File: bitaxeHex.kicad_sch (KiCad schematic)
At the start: 8 parts, among them J1 Conn_01x01, J2 Conn_01x01

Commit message: hex initial import
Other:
- sheet BM1397 renamed BM1397-1
- added sheet BM1397-3 (bm1397-3.kicad_sch)
- added sheet BM1398-2 (bm1397-2.kicad_sch)
- sheet BM1397-1: file bm1397.kicad_sch -> bm1397-1.kicad_sch
- sheet Fan ports: added TEMP1_N, TEMP1_P, TEMP2_N, TEMP2_P; removed TEMP_N, TEMP_P
- title: le bitaxeMax -> bitaxeHex
- moved on the sheet: H1, H2, H3, H4, H5, H6

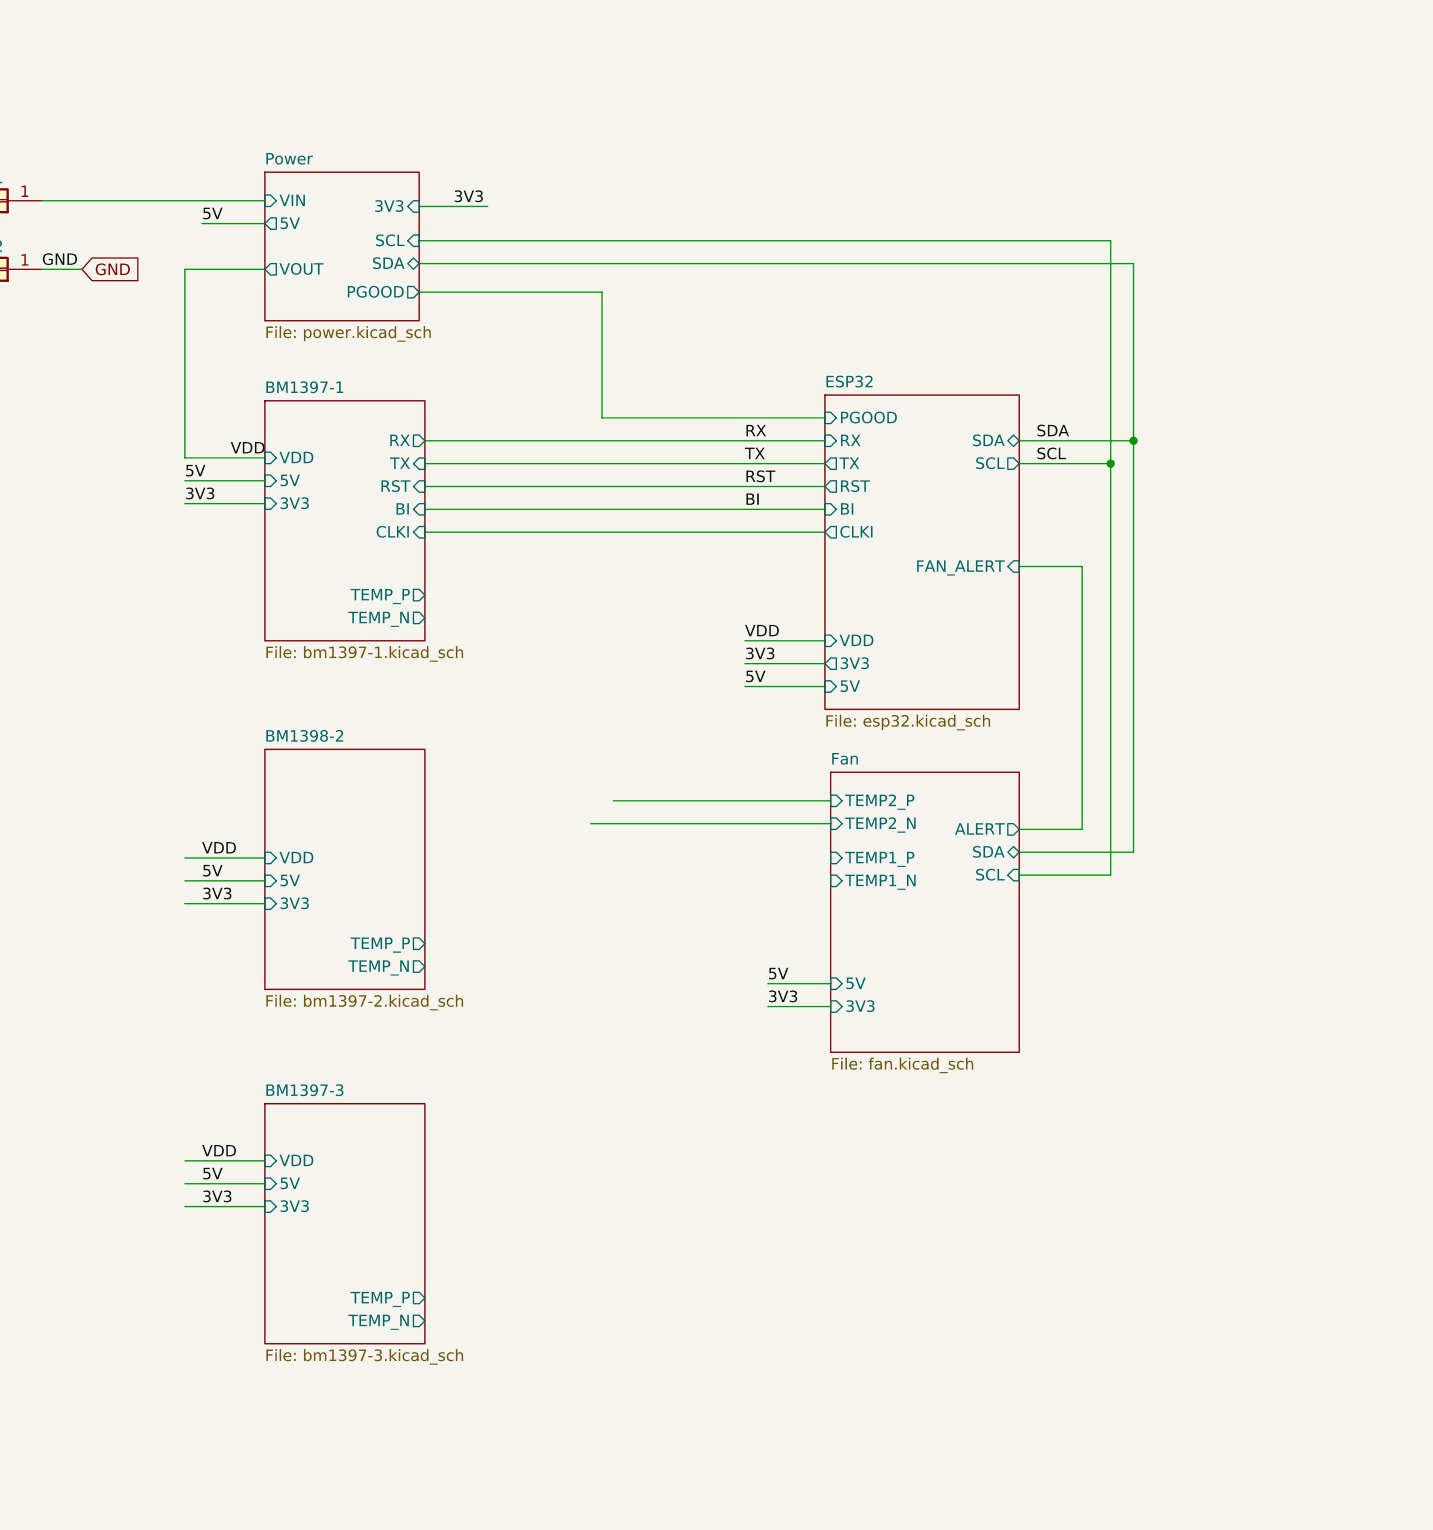
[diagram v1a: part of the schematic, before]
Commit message: connected up power and data to ASICs in schematic
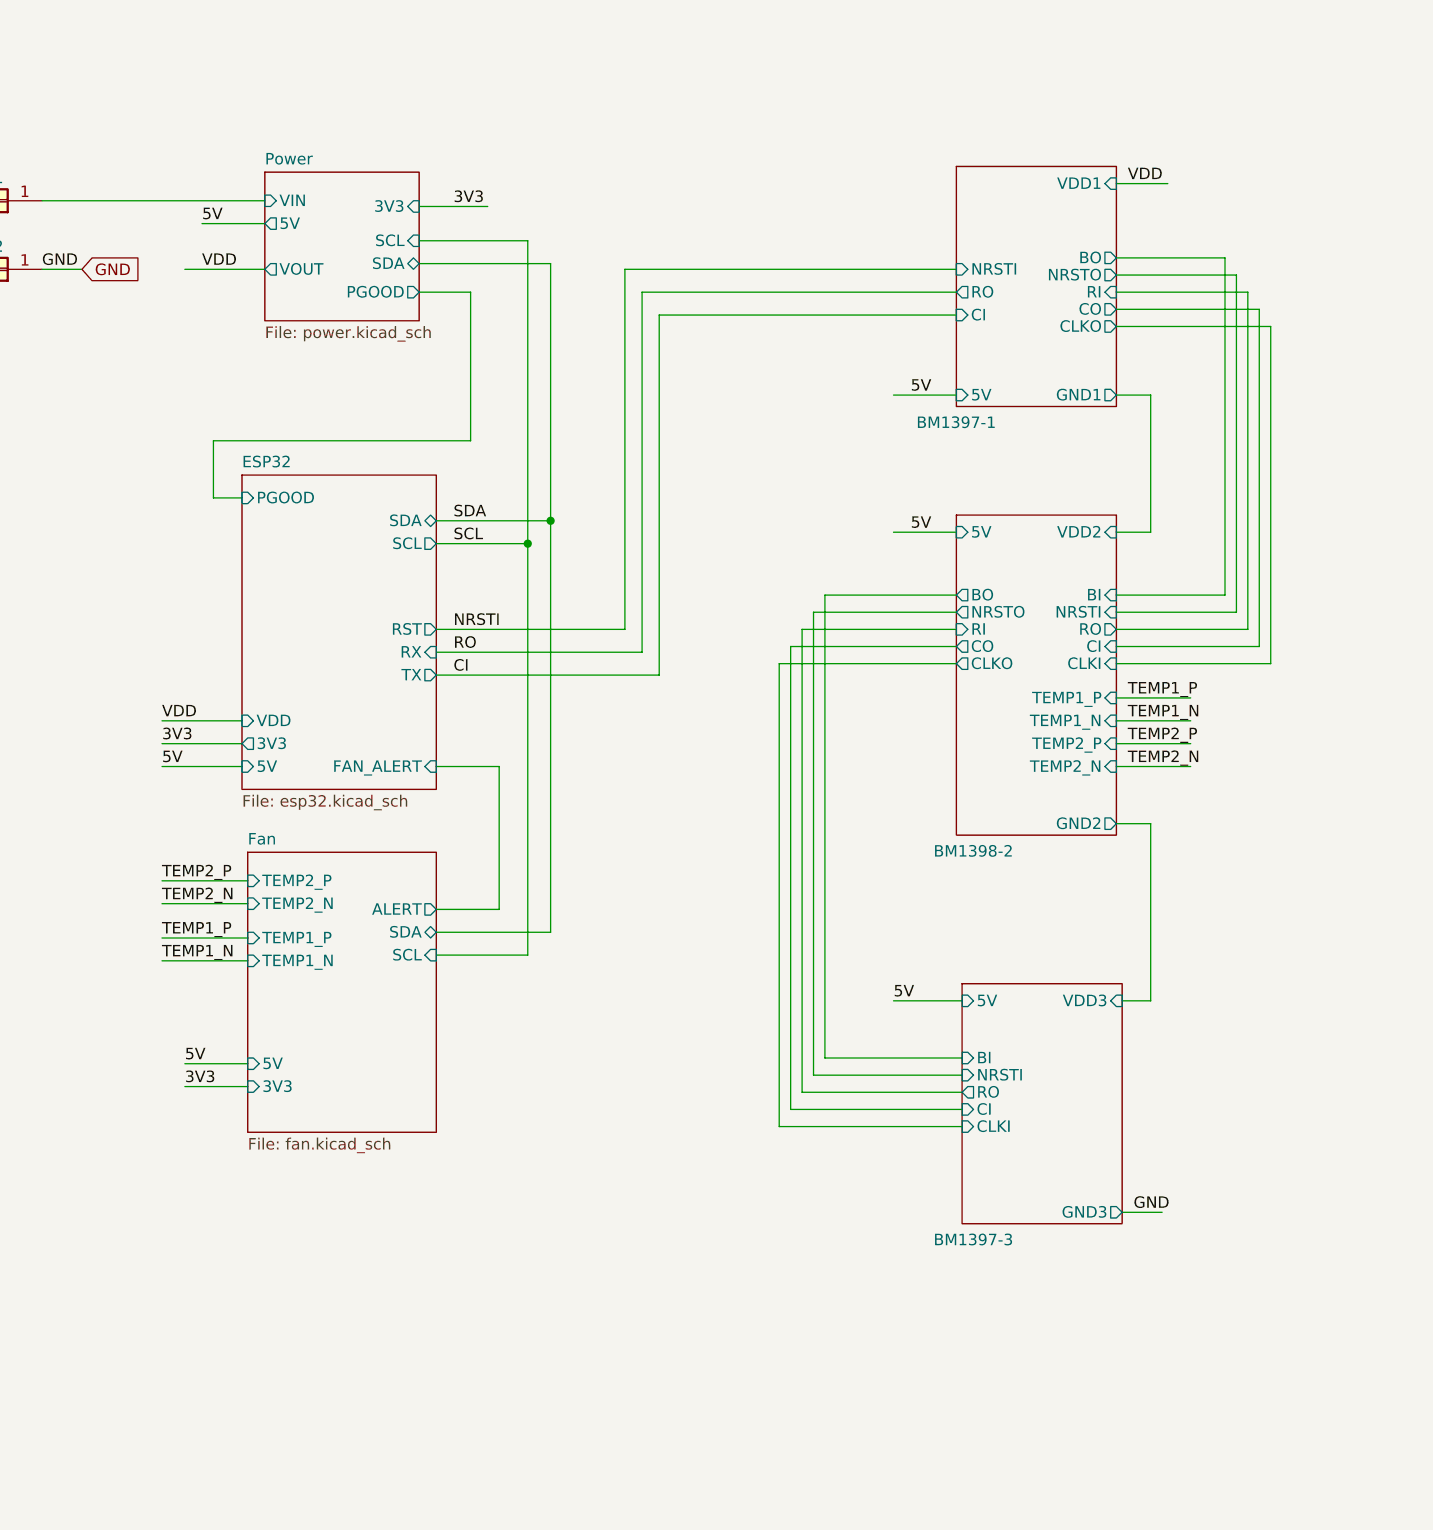
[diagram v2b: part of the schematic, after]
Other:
- sheet BM1397-1 ports: added BO, CI, CLKO, CO, GND1, NRSTI, NRSTO, RI, RO, VDD1; removed 3V3, BI, CLKI, RST, RX, TEMP_N, TEMP_P, TX, VDD
- sheet BM1397-3 ports: added BI, CI, CLKI, GND3, NRSTI, RO, VDD3; removed 3V3, TEMP_N, TEMP_P, VDD
- sheet BM1398-2 ports: added BI, BO, CI, CLKI, CLKO, CO, GND2, NRSTI, NRSTO, RI, RO, TEMP1_N, TEMP1_P, TEMP2_N, TEMP2_P, VDD2; removed 3V3, TEMP_N, TEMP_P, VDD
- sheet ESP32 ports: added none; removed BI, CLKI

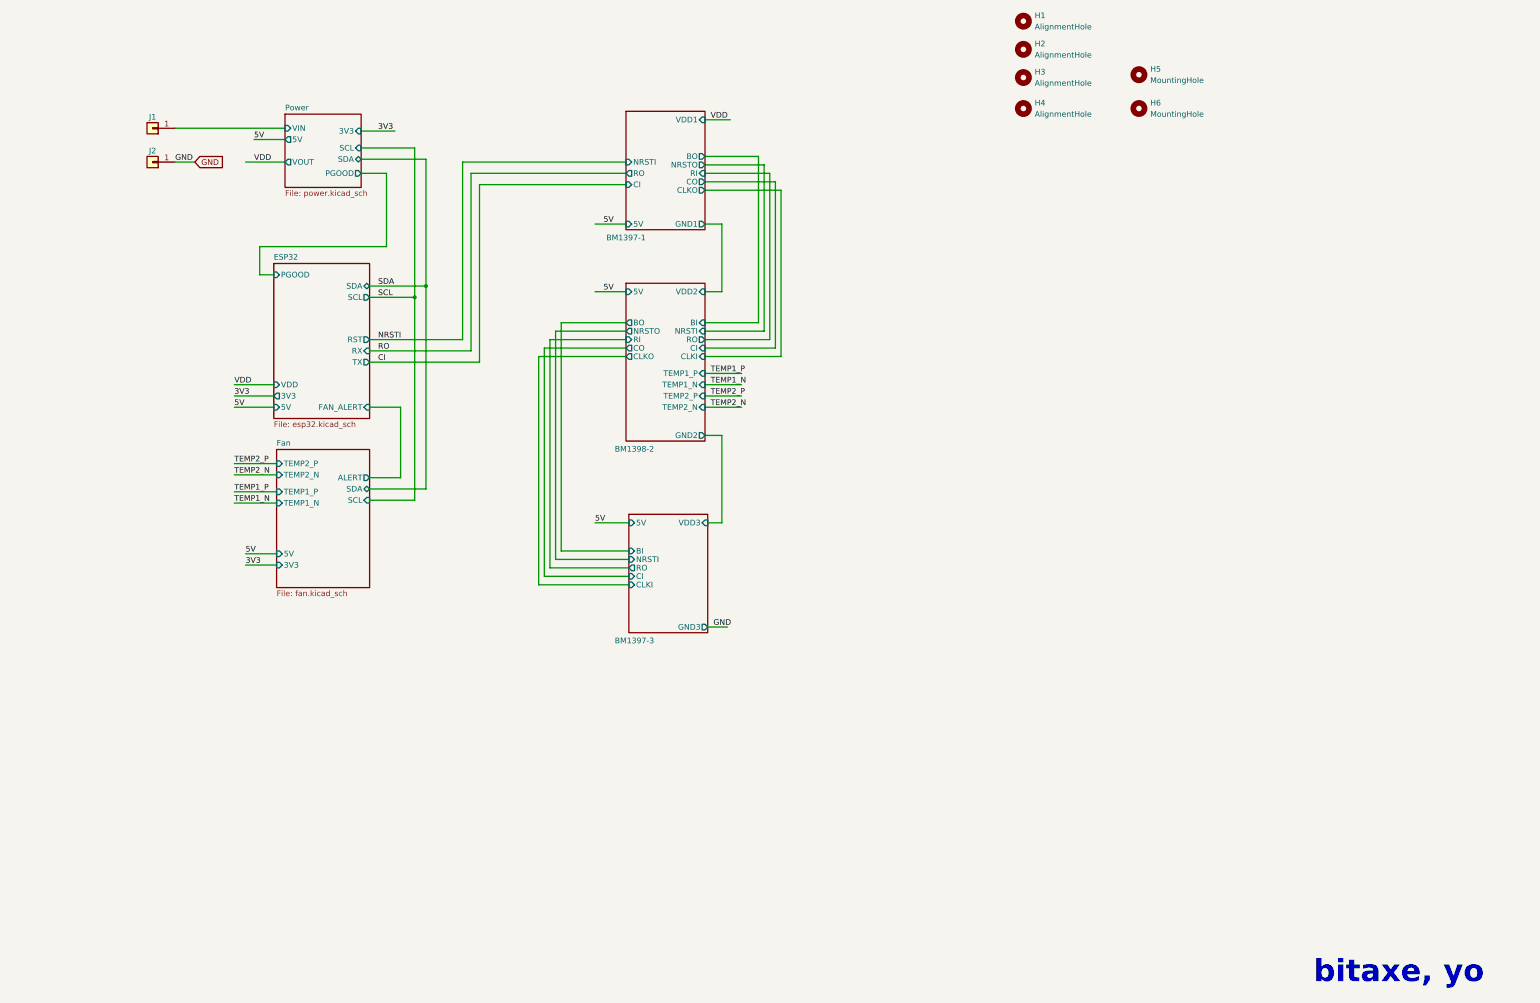
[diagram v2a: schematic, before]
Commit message: fixed the floating gnd net issue. started placement
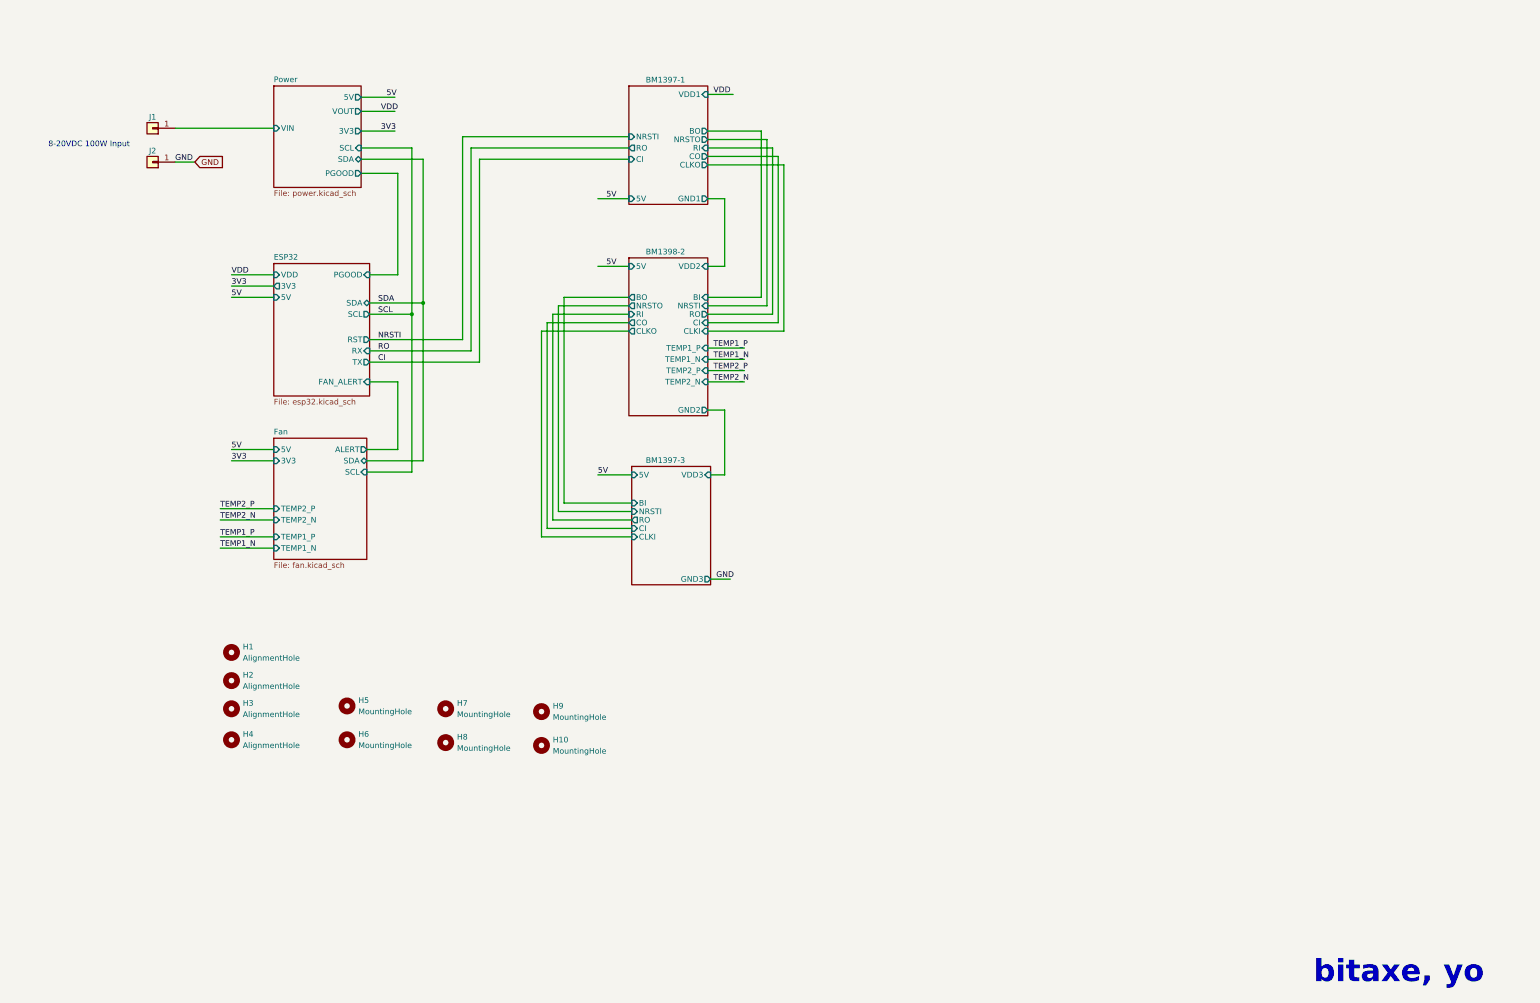
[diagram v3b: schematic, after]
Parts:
- added H10, H7, H8, H9: MountingHole, MountingHole:MountingHole_3.5mm, symbol Mechanical:MountingHole
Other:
- note added: "8-20VDC 100W Input"
- moved on the sheet: H1, H2, H3, H4, H5, H6

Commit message: some more placements, added level shifters..
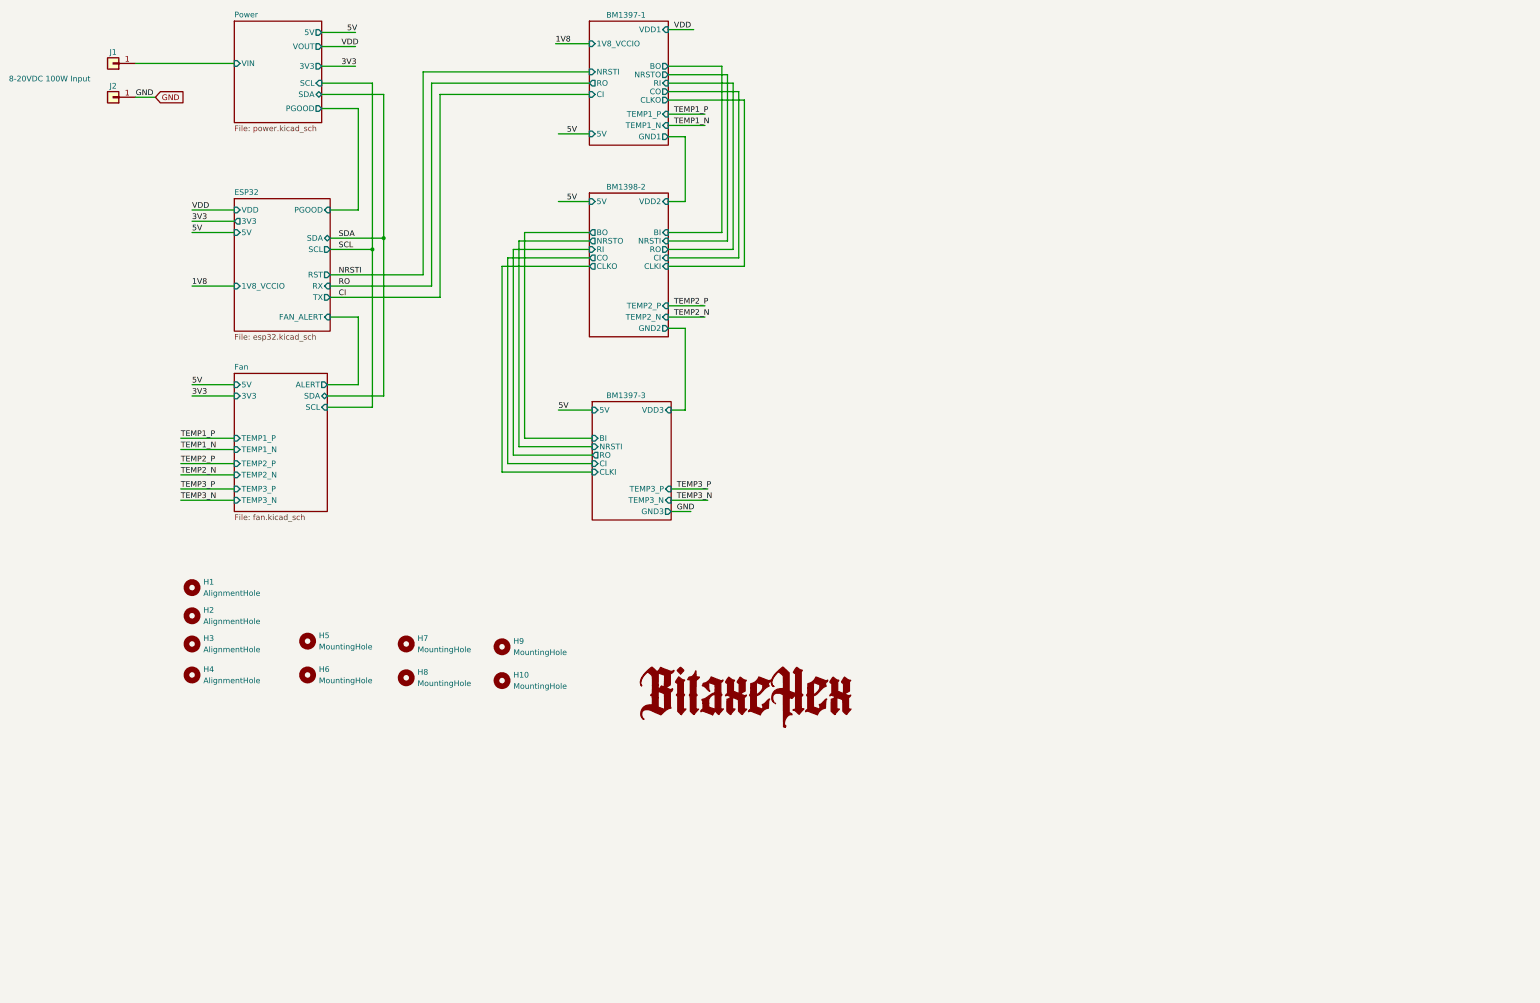
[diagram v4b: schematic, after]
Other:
- sheet BM1397-1 ports: added 1V8_VCCIO, TEMP1_N, TEMP1_P; removed none
- sheet BM1397-3 ports: added TEMP3_N, TEMP3_P; removed none
- sheet BM1398-2 ports: added none; removed TEMP1_N, TEMP1_P
- sheet ESP32 ports: added 1V8_VCCIO; removed none
- sheet Fan ports: added TEMP3_N, TEMP3_P; removed none
- note removed: "bitaxe, yo"
- moved on the sheet: H1, H10, H2, H3, H4, H5, H6, H7, H8, H9, J1, J2

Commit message: small fixes
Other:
- sheet BM1398-2 renamed BM1397-2
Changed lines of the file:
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@@
     (stroke (width 0.1524) (type solid))
     (fill (color 255 255 194 1.0000))
-    (property "Sheetname" "BM1398-2" (at 154.94 66.675 0)
+    (property "Sheetname" "BM1397-2" (at 154.94 66.675 0)
       (effects (font (size 1.27 1.27)) (justify left bottom))
     )
